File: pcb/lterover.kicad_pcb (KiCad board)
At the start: 2 copper layers, 37 x 28 mm, 0 parts

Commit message: Finished schematic and layout
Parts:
- added BT1: Battery, Library:battery_2pad, F.Cu at (111.9, 96.6)
- added C1: 220n, Capacitor_SMD:C_0402_1005Metric, F.Cu at (126.4, 109.4)
- added C10: 220n, Capacitor_SMD:C_0402_1005Metric, F.Cu at (133.9, 103.9)
- added C11: 1u, Capacitor_SMD:C_0402_1005Metric, F.Cu at (131.9, 97.7)
- added C12: 2.2u, Capacitor_SMD:C_0603_1608Metric, F.Cu at (114.6, 100.2)
- added C13: 1u, Capacitor_SMD:C_0402_1005Metric, F.Cu at (125.9, 100.2)
- added C2: 220n, Capacitor_SMD:C_0402_1005Metric, F.Cu at (133.8, 109.9)
- added C3: 470n, Capacitor_SMD:C_0402_1005Metric, F.Cu at (124.5, 115.4)
- added C4: 220n, Capacitor_SMD:C_0402_1005Metric, F.Cu at (119.1, 109.6)
- added C5: 10n, Capacitor_SMD:C_0201_0603Metric, F.Cu at (120.5, 115.7)
- added C6: 10n, Capacitor_SMD:C_0201_0603Metric, F.Cu at (118.7, 111.4)
- added C7: 100u, Capacitor_SMD:CP_Elec_5x5.4, F.Cu at (114.6, 105.5)
- added C8: 22n, Capacitor_SMD:C_0201_0603Metric, F.Cu at (120.9, 109.3)
- added C9: 220n, Capacitor_SMD:C_0402_1005Metric, F.Cu at (134.8, 102.1)
- added D1: LED, LED_SMD:LED_0402_1005Metric, F.Cu at (126.0, 96.2)
- added D2: LED, LED_SMD:LED_0402_1005Metric, F.Cu at (128.3, 114.0)
- added D3: LED, LED_SMD:LED_0402_1005Metric, F.Cu at (129.8, 114.0)
- added J1: Conn_02x03_Odd_Even, Connector_PinHeader_1.00mm:PinHeader_2x03_P1.00mm_Vertical, F.Cu at (136.7, 114.1)
- added J2: Conn_01x02_Socket, Connector_JST:JST_XH_B2B-XH-A_1x02_P2.50mm_Vertical, F.Cu at (114.3, 111.9)
- added R1: 10k, Resistor_SMD:R_0402_1005Metric, F.Cu at (140.0, 115.8)
- added R2: 10k, Resistor_SMD:R_0402_1005Metric, F.Cu at (135.9, 99.3)
- added R3: 10k, Resistor_SMD:R_0402_1005Metric, F.Cu at (135.9, 98.0)
- added R4: 200, Resistor_SMD:R_0402_1005Metric, F.Cu at (126.0, 94.0)
- added R5: 200, Resistor_SMD:R_0402_1005Metric, F.Cu at (128.3, 116.3)
- added R6: 200, Resistor_SMD:R_0402_1005Metric, F.Cu at (129.8, 116.3)
- added SW1: SW_Push, Button_Switch_THT:SW_PUSH_6mm, F.Cu at (139.9, 110.7)
- added U1: DRV8256E, Package_DFN_QFN:VQFN-24-1EP_4x4mm_P0.5mm_EP2.5x2.5mm_ThermalVias, F.Cu at (121.8, 112.5)
- added U2: ATmega328PB-M, Package_DFN_QFN:QFN-32-1EP_5x5mm_P0.5mm_EP3.1x3.1mm, F.Cu at (130.1, 109.4)
- added U3: BNO055, Package_LGA:LGA-28_5.2x3.8mm_P0.5mm, F.Cu at (131.1, 101.0)
- added U4: BD33FC0FP, Package_TO_SOT_SMD:TO-252-2, F.Cu at (120.2, 95.2)

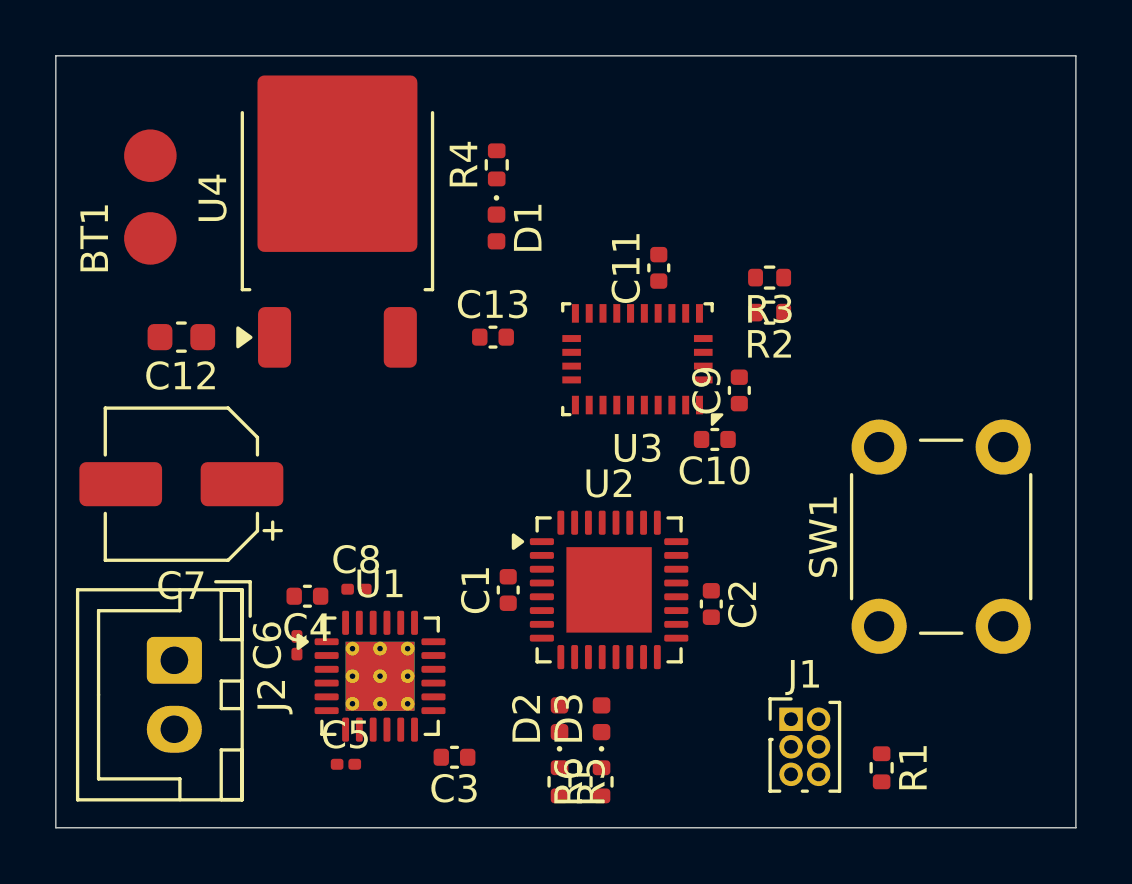
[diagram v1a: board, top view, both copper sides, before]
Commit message: Finished PCB routing, deleted server for new project
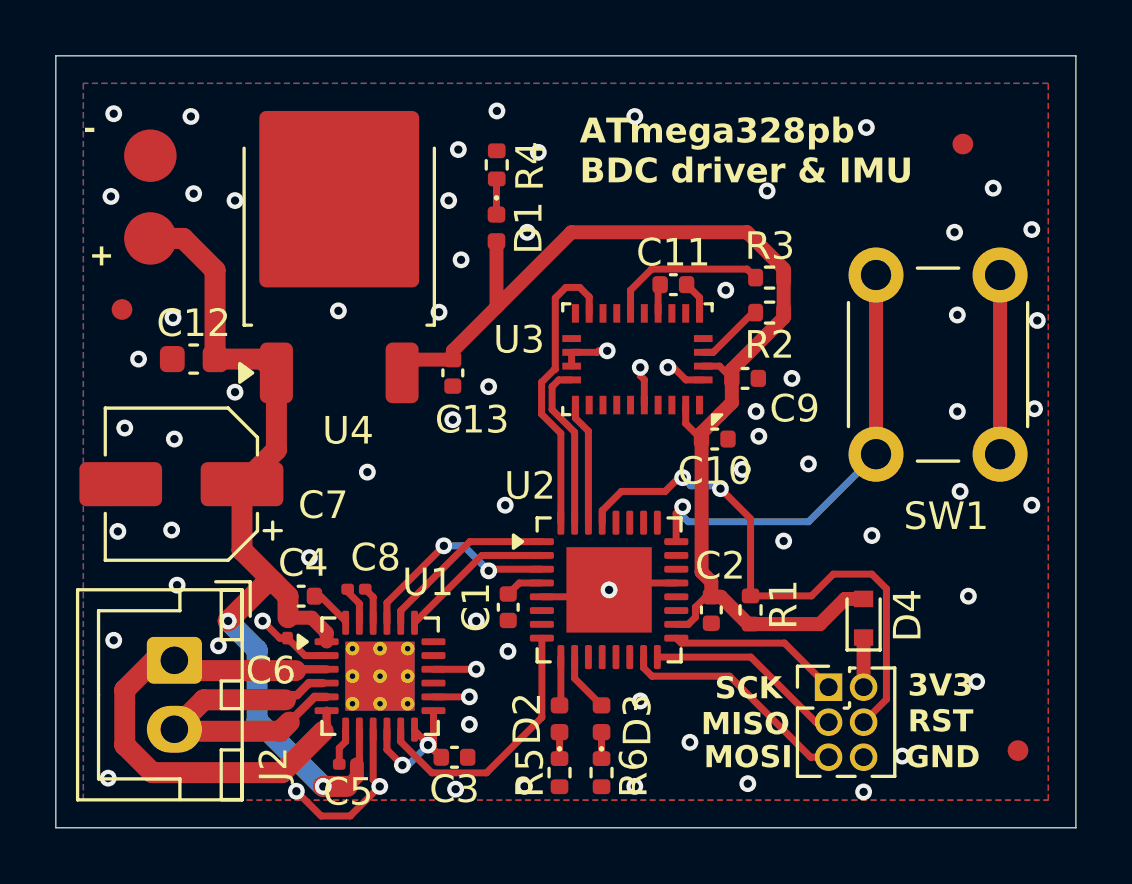
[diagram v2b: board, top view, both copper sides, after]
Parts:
- added D4: ~, Diode_SMD:D_SOD-523, F.Cu at (139.3, 110.4)
- added FID1: Fiducial, Fiducial:Fiducial_0.75mm_Mask1.5mm, F.Cu at (142.9, 93.2)
- added FID2: Fiducial, Fiducial:Fiducial_0.75mm_Mask1.5mm, F.Cu at (144.9, 115.2)
- added FID3: Fiducial, Fiducial:Fiducial_0.75mm_Mask1.5mm, F.Cu at (112.4, 99.2)
- J1: footprint Connector_PinHeader_1.00mm:PinHeader_2x03_P1.00mm_Vertical -> Connector_PinHeader_1.27mm:PinHeader_2x03_P1.27mm_Vertical
- moved R1 7.44 mm to (135.2, 110.1), turned to 90 degrees
- moved SW1 6.24 mm to (139.8, 104.5)
- moved C13 1.95 mm to (124.4, 101.5), turned to -90 degrees
- moved J1 1.79 mm to (138.0, 112.9)
- moved U4 1.29 mm to (120.3, 96.5)
- moved C12 0.91 mm to (115.0, 101.0)
- moved C11 0.81 mm to (132.4, 98.3), turned to 0 degrees
- moved C6 0.67 mm to (118.4, 110.8)
- moved C1 0.62 mm to (126.4, 110.0)
- moved C9 0.48 mm to (135.0, 101.7), turned to 180 degrees
- moved R6 0.33 mm to (129.8, 116.0), turned to -90 degrees
- moved R5 0.33 mm to (128.3, 116.0)
- moved C4 0.23 mm to (118.9, 109.6)
- moved C2 0.22 mm to (133.8, 110.1), turned to 90 degrees
- moved C5 0.08 mm to (120.6, 115.7)
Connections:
- J1 pad 1: /MISO -> /SCK
- J1 pad 2: +3.3V -> /VOUT
- J1 pad 3: /SCK -> /MISO
- J1 pad 4: /MOSI -> RESETB
- J1 pad 5: RESETB -> /MOSI
- U2 pad 24: unconnected-(U2-PC1-Pad24) -> /BTN
- U2 pad 28: /BTN -> unconnected-(U2-PC5-Pad28)
- U3 pad 19: USART1_RX -> USART1_TX
- U3 pad 20: USART1_TX -> USART1_RX
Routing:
- net +3.3V: track 0.00 -> 44.7 mm
- net +7.5V: track 0.00 -> 33.4 mm, vias 0 -> 2
- net GND: track 0.00 -> 30.6 mm, vias 0 -> 71
- net RESETB: track 0.00 -> 20.4 mm, vias 0 -> 2
- net /M1: track 0.00 -> 19.0 mm
- net /BTN: track 0.00 -> 17.1 mm, vias 0 -> 1
- net /M2: track 0.00 -> 12.4 mm
- net IMU_INT: track 0.00 -> 10.8 mm
- net BDC_INT: track 0.00 -> 9.73 mm
- net /MOSI: track 0.00 -> 8.44 mm
- net BDC_SLP: track 0.00 -> 7.60 mm, vias 0 -> 2
- net /MISO: track 0.00 -> 7.19 mm
- net BDC_EN: track 0.00 -> 6.60 mm
- net /SCK: track 0.00 -> 6.26 mm
- net USART1_TX: track 0.00 -> 6.08 mm
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- added copper zone on B.Cu, net GND
- added copper zone on F.Cu, net GND
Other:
- board text added: "+"
- board text added: "-"
- board text added: "3V3"
- board text added: "ATmega328pb BDC driver & IMU"
- board text added: "GND"
- board text added: "MISO"
- board text added: "MOSI"
- board text added: "RST"
- board text added: "SCK"

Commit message: Finished PCB
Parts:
- J1: footprint Connector_PinHeader_1.27mm:PinHeader_2x03_P1.27mm_Vertical -> Connector_PinHeader_2.54mm:PinHeader_2x03_P2.54mm_Vertical
- moved R1 3.16 mm to (136.9, 107.4)
- moved D4 2.45 mm to (139.4, 108.0), turned to 180 degrees
- moved J1 2.19 mm to (138.4, 110.7)
- moved FID2 1.77 mm to (145.8, 116.8)
- moved D2 0.16 mm to (128.3, 114.2)
- moved D3 0.05 mm to (129.8, 114.1)
- turned C2 to -90 degrees
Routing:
- net GND: track 30.6 -> 108.6 mm, vias 71 -> 41
- net +3.3V: track 44.7 -> 58.9 mm, vias 0 -> 2
- net RESETB: track 20.4 -> 17.6 mm
- net /VOUT: track 1.80 -> 2.88 mm
- removed copper zone on F.Cu, net GND
